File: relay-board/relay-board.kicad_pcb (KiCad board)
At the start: 2 copper layers, 149.9 x 88.9 mm, 82 parts, among them IC1 OPTO-TRANSISTOR4, IC2 OPTO-TRANSISTOR4, IC3 OPTO-TRANSISTOR4, IC4 OPTO-TRANSISTOR4, IC5 OPTO-TRANSISTOR4, IC6 OPTO-TRANSISTOR4, IC7 OPTO-TRANSISTOR4, IC8 OPTO-TRANSISTOR4, K1 RELAY_JS5N-K, K10 CONN_01X03, K11 CONN_01X03, K12 CONN_01X03, K13 CONN_01X03, K14 CONN_01X03, K15 CONN_01X03, K16 CONN_01X03, K2 RELAY_JS5N-K, K3 RELAY_JS5N-K, K4 RELAY_JS5N-K, K5 RELAY_JS5N-K, K6 RELAY_JS5N-K, K7 RELAY_JS5N-K, K8 RELAY_JS5N-K, K9 CONN_01X03, P1 CONN_01X04, P2 CONN_01X04, P3 CONN_02X03, P4 CONN_01X02, P5 CONN_01X02, P6 CONN_01X02, P7 CONN_01X02, Q1 BS107, Q2 BS107, Q3 BS107, Q4 BS107, Q5 BS107, Q6 BS107, Q7 BS107, Q8 BS107, U1 PCF8574

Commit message: [relay-board] Updated and polished PCB (to version 1.1)
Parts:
- added Ref**: Val**, screw-pad, F.Cu at (89.5, 149.2)
- added Ref**: Val**, screw-pad, F.Cu at (230.5, 149.2)
- Ref** (x6): footprint pad -> screw-pad
- moved P7 7.01 mm to (228.0, 142.9)
- moved P6 7.01 mm to (228.0, 136.5)
- moved P5 6.99 mm to (221.6, 142.9)
- moved Ref** 6.99 mm to (89.5, 163.2)
- moved Ref** 6.99 mm to (230.5, 163.2)
- moved P4 6.98 mm to (221.6, 136.5)
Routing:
- net DGND: track 290.7 -> 282.1 mm
- net +5VD: track 369.6 -> 376.5 mm
- net N-0000064: track 11.1 -> 10.4 mm
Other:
- board text added: "SIMPLE RelayBoard v1.1"
- board text removed: "SIMPLE RelayBoard v1.0"

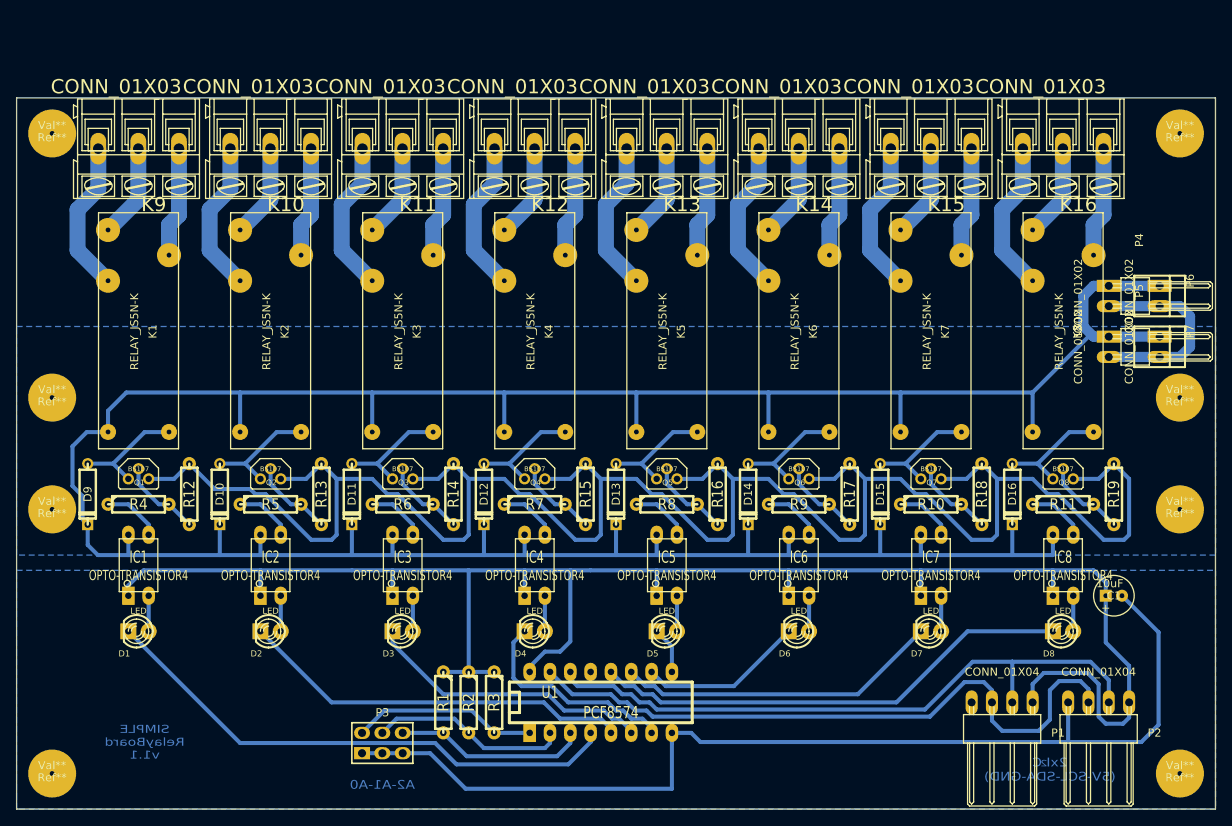
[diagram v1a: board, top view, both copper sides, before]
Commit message: [relay-board] Screw holes enlarged and rearranged.
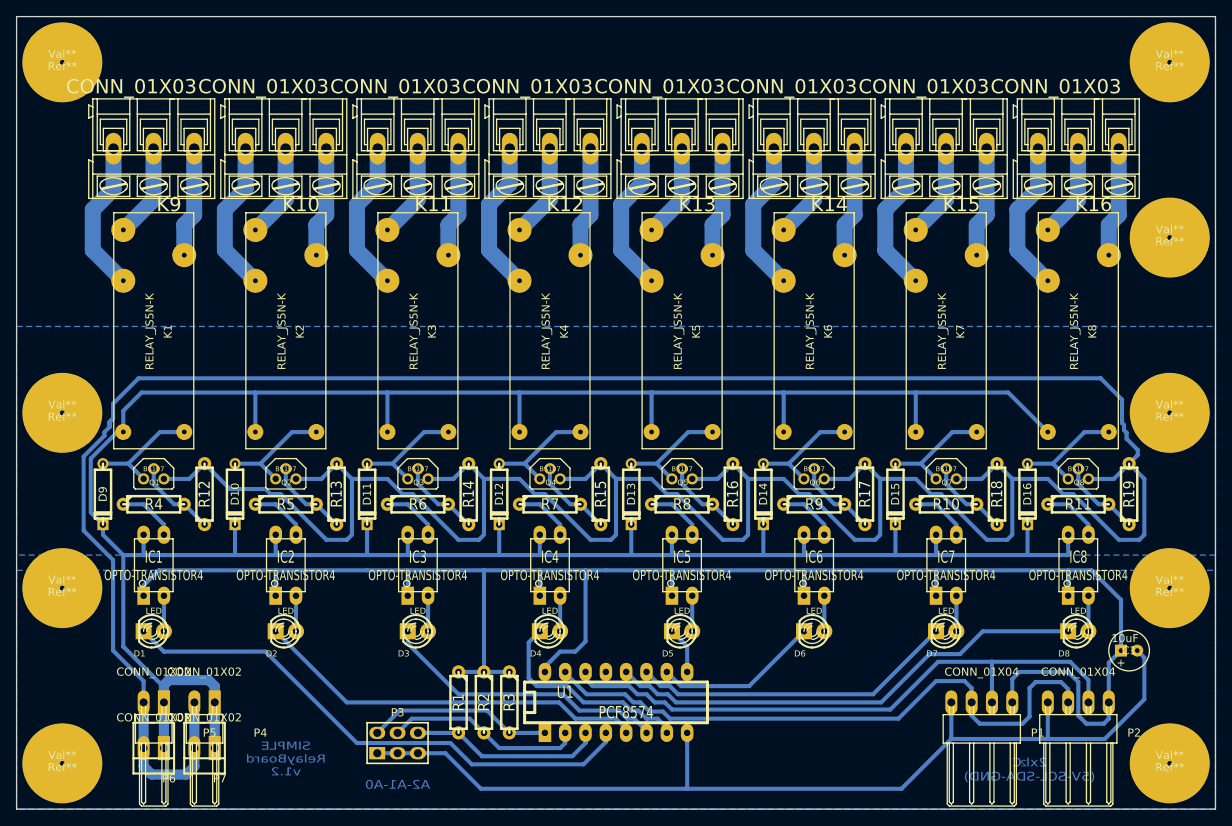
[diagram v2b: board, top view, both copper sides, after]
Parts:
- added Ref**: Val**, screw-pad, F.Cu at (229.2, 151.1)
- moved P6 137.8 mm to (102.2, 193.0), turned to 180 degrees
- moved P7 129.5 mm to (108.6, 193.0), turned to 180 degrees
- moved P5 127.4 mm to (102.2, 187.3), turned to 180 degrees
- moved P4 123.9 mm to (108.6, 187.3), turned to 180 degrees
- moved Ref** 20.0 mm to (229.2, 129.2)
- moved Ref** 9.92 mm to (90.8, 173.0)
- moved Ref** 9.92 mm to (229.2, 173.0)
- moved Ref** 8.98 mm to (90.8, 107.3)
- moved Ref** 8.98 mm to (229.2, 107.3)
- moved C1 7.12 mm to (224.2, 180.8)
- moved P1 2.54 mm to (205.7, 187.3)
- moved P2 2.54 mm to (217.8, 187.3)
- moved Ref** 2.29 mm to (90.8, 151.1)
- moved D1 1.91 mm to (102.2, 178.4)
- moved D10 1.91 mm to (112.4, 161.3)
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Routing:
- net DGND: track 282.1 -> 461.1 mm
- net GND: track 132.7 -> 125.5 mm
- net N-0000036: track 83.0 -> 77.8 mm
- net N-0000035: track 82.2 -> 77.8 mm
- net +5VD: track 376.5 -> 378.2 mm
- net +5V: track 220.4 -> 219.2 mm
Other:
- board size 149.9 x 88.9 mm -> 149.9 x 99.1 mm
- board text added: "SIMPLE RelayBoard v1.2"
- board text removed: "SIMPLE RelayBoard v1.1"

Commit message: [relay-board] Updated PCB.
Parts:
- removed the Ref** at (229.2, 107.3)
- moved Ref** 21.9 mm to (90.8, 129.2)
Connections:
- K1 pad 1: N-0000031 -> N-0000020
- K1 pad 2: N-0000030 -> N-0000021
- K10 pad 2: N-0000038 (its old number) -> N-0000029
- K10 pad 3: N-0000046 (its old number) -> N-0000028
- K11 pad 2: N-0000040 (its old number) -> N-0000027
- K11 pad 3: N-0000045 (its old number) -> N-0000030
- K12 pad 2: N-0000042 (its old number) -> N-0000012
- K12 pad 3: N-0000033 (its old number) -> N-0000031
- K13 pad 2: N-0000016 (its old number) -> N-000009
- K13 pad 3: N-0000012 -> N-0000018
- K14 pad 2: N-0000010 (its old number) -> N-0000015
- K14 pad 3: N-0000015 -> N-0000017
- K15 pad 3: N-000003 (its old number) -> N-0000025
- K16 pad 2: N-000008 (its old number) -> N-000007
- K16 pad 3: N-000007 -> N-0000026
- K2 pad 1: N-0000038 (its old number) -> N-0000028
- K2 pad 2: N-0000046 (its old number) -> N-0000029
- K3 pad 1: N-0000040 (its old number) -> N-0000030
- K3 pad 2: N-0000045 (its old number) -> N-0000027
- K4 pad 1: N-0000042 (its old number) -> N-0000031
- K4 pad 2: N-0000033 (its old number) -> N-0000012
- K5 pad 1: N-0000016 (its old number) -> N-0000018
- K5 pad 2: N-0000012 -> N-000009
- K6 pad 1: N-0000010 (its old number) -> N-0000017
- K7 pad 1: N-000004 -> N-0000025
- K7 pad 2: N-000003 (its old number) -> N-000004
- K8 pad 1: N-000008 (its old number) -> N-0000026
- K9 pad 2: N-0000031 -> N-0000021
- K9 pad 3: N-0000030 -> N-0000020
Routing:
- net N-0000046 (its old number): track 19.2 -> 0.00 mm
- net N-0000033 (its old number): track 19.2 -> 0.00 mm
- net N-000003 (its old number): track 19.2 -> 0.00 mm
- net N-0000045 (its old number): track 19.2 -> 0.00 mm
- net N-0000021: track 0.00 -> 18.1 mm
- net N-0000027: track 0.00 -> 18.1 mm
- net N-0000029: track 0.00 -> 18.1 mm
- net N-000009: track 0.00 -> 18.1 mm
- net N-0000040 (its old number): track 11.7 -> 0.00 mm
- net N-0000010 (its old number): track 11.7 -> 0.00 mm
- net N-0000038 (its old number): track 11.7 -> 0.00 mm
- net N-000008 (its old number): track 11.7 -> 0.00 mm
- net N-0000042 (its old number): track 11.7 -> 0.00 mm
- net N-0000016 (its old number): track 11.7 -> 0.00 mm
- net N-0000028: track 0.00 -> 10.7 mm
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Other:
- board size 149.9 x 99.1 mm -> 149.9 x 89.5 mm
- net class Default: trace_width 0.508 -> 2
- board text added: "SIMPLE RelayBoard v1.3"
- board text removed: "SIMPLE RelayBoard v1.2"
